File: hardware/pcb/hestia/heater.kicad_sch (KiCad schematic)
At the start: 23 parts, among them Q1 FDS8876, SW2 SW_Push_Open, U10 INA826

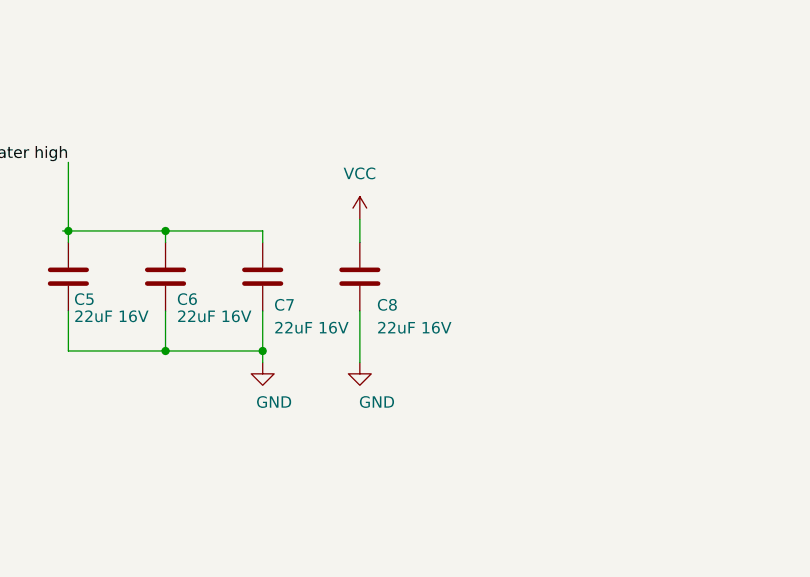
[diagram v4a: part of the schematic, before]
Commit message: pcb: move C8 to buck_converter schematic, removed some outdated comments
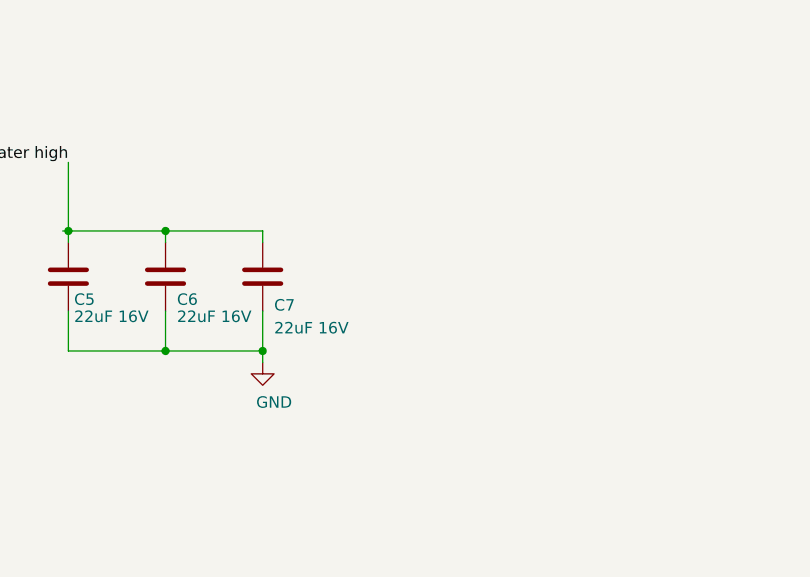
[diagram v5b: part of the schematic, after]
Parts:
- removed C8: 22uF 16V, Capacitor_SMD:C_1206_3216Metric, symbol Device:C
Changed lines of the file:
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@@
-    (stroke (width 0) (type default) (color 0 0 0 0))
-  )
-  (wire (pts (xy 239.395 57.785) (xy 239.395 60.325))
     (stroke (width 0) (type default) (color 0 0 0 0))
   )
@@
   )
   (wire (pts (xy 217.805 67.945) (xy 217.805 72.39))
-    (stroke (width 0) (type default) (color 0 0 0 0))
-  )
-  (wire (pts (xy 239.395 67.945) (xy 239.395 73.66))
     (stroke (width 0) (type default) (color 0 0 0 0))
   )
@@
     (pin "1")
   )
-  (symbol (lib_id "power:VCC") (at 239.395 57.785 0) (unit 1)
-    (in_bom yes) (on_board yes) (fields_autoplaced)
-    (property "Reference" "#PWR07" (id 0) (at 239.395 61.595 0)
-      (effects (font (size 1.27 1.27)) hide)
-    )
-    (property "Value" "VCC" (id 1) (at 239.395 52.705 0))
-    (property "Footprint" "" (id 2) (at 239.395 57.785 0)
-      (effects (font (size 1.27 1.27)) hide)
-    )
-    (property "Datasheet" "" (id 3) (at 239.395 57.785 0)
-      (effects (font (size 1.27 1.27)) hide)
-    )
-    (pin "1")
-  )
   (symbol (lib_id "power:VCC") (at 129.54 73.66 0) (unit 1)
     (in_bom yes) (on_board yes) (fields_autoplaced)
@@
     )
     (pin "1")
-  )
-  (symbol (lib_id "Device:C") (at 239.395 64.135 0) (unit 1)
-    (in_bom yes) (on_board yes)
-    (property "Reference" "C8" (id 0) (at 241.3 67.31 0)
-      (effects (font (size 1.27 1.27)) (justify left))
-    )
-    (property "Value" "22uF 16V" (id 1) (at 241.3 69.85 0)
-      (effects (font (size 1.27 1.27)) (justify left))
-    )
-    (property "Footprint" "Capacitor_SMD:C_1206_3216Metric" (id 2) (at 240.3602 67.945 0)
-      (effects (font (size 1.27 1.27)) hide)
-    )
-    (property "Datasheet" "~" (id 3) (at 239.395 64.135 0)
-      (effects (font (size 1.27 1.27)) hide)
-    )
-    (property "LCSC Part" "C13585" (id 4) (at 239.395 64.135 0)
-      (effects (font (size 1.27 1.27)) hide)
-    )
-    (pin "1")
-    (pin "2")
   )
   (symbol (lib_id "Device:R") (at 106.045 122.555 90) (unit 1)
@@
     (pin "2")
   )
-  (symbol (lib_id "power:GND") (at 239.395 73.66 0) (unit 1)
-    (in_bom yes) (on_board yes)
-    (property "Reference" "#PWR08" (id 0) (at 239.395 80.01 0)
-      (effects (font (size 1.27 1.27)) hide)
-    )
-    (property "Value" "GND" (id 1) (at 241.3 78.105 0))
-    (property "Footprint" "" (id 2) (at 239.395 73.66 0)
-      (effects (font (size 1.27 1.27)) hide)
-    )
-    (property "Datasheet" "" (id 3) (at 239.395 73.66 0)
-      (effects (font (size 1.27 1.27)) hide)
-    )
-    (pin "1")
-  )
 )

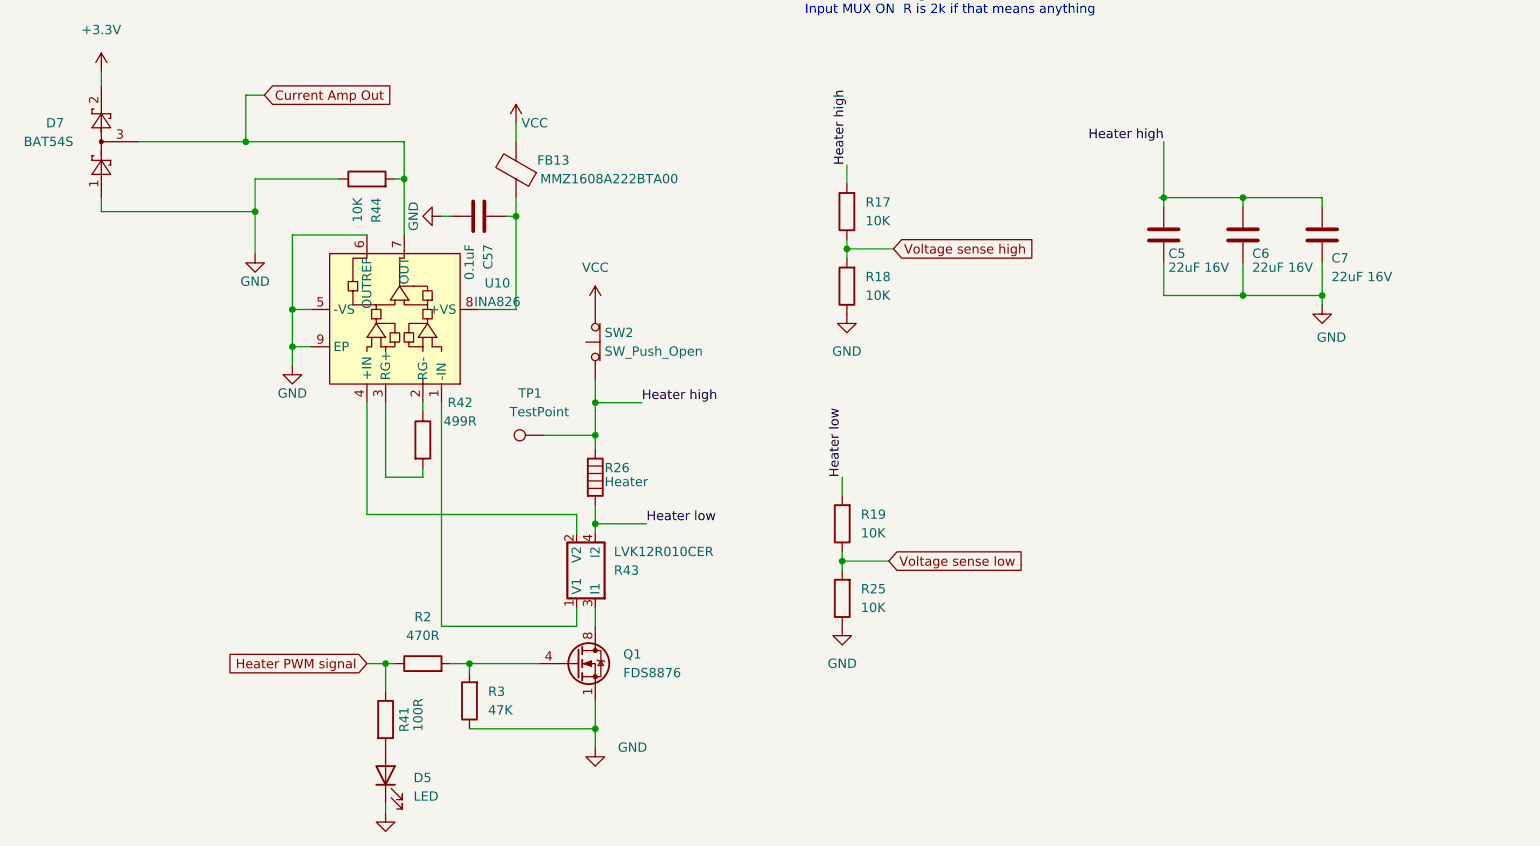
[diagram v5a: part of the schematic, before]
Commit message: added some digikey and mouser part numbers to schematic parts
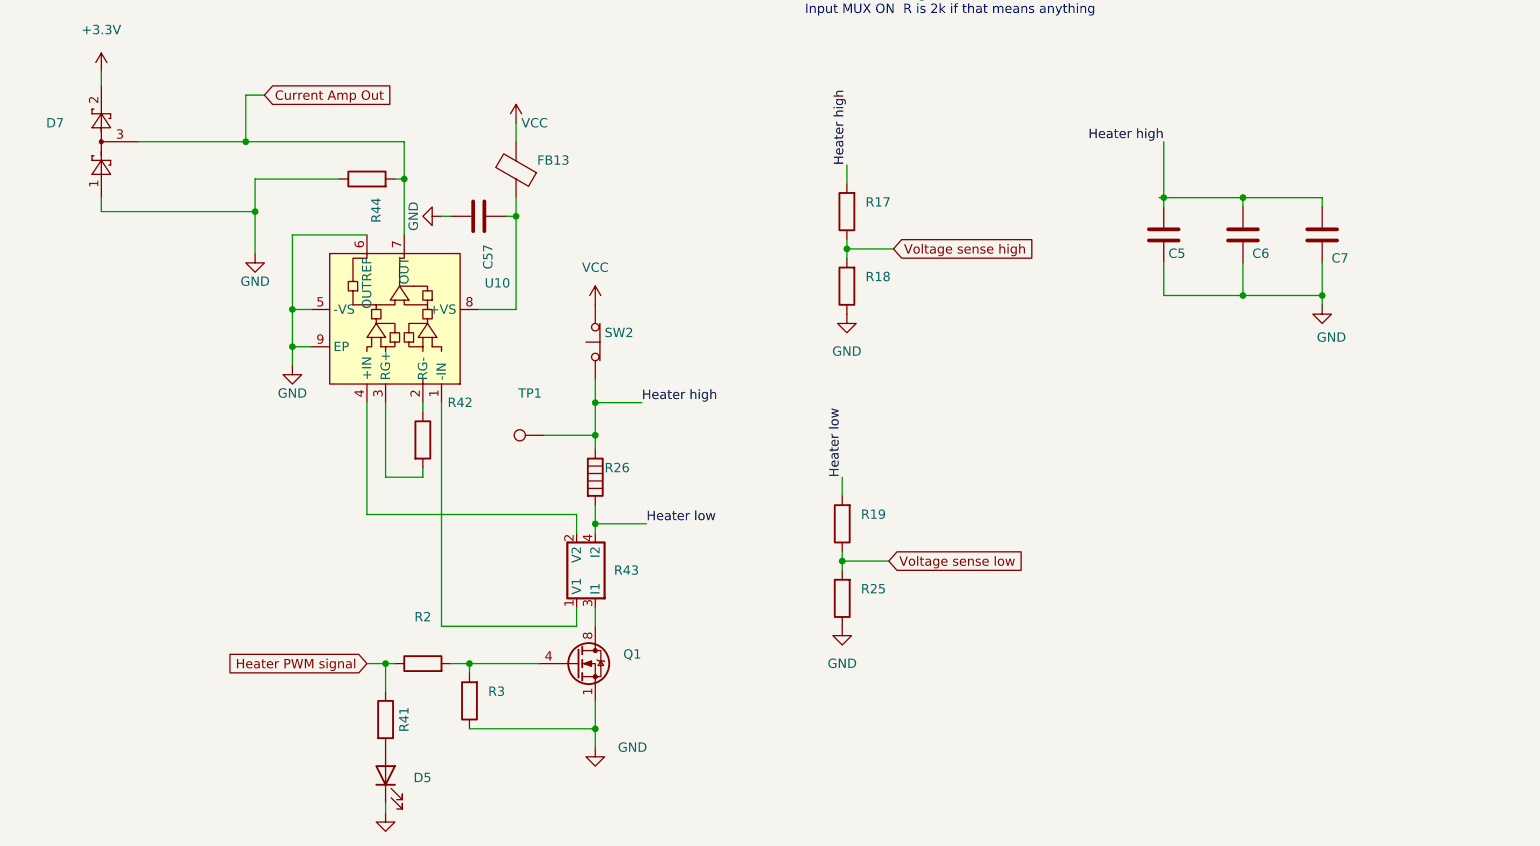
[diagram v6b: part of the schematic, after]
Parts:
- C5, C6, C7: value 22uF 16V -> (none); footprint Capacitor_SMD:C_1206_3216Metric -> (none); Digikey Part (none) -> 1276-2728-1-ND
- C57: value 0.1uF -> (none); footprint Capacitor_SMD:C_0603_1608Metric_Pad1.08x0.95mm_HandSolder -> (none)
- D5: value LED -> (none); footprint LED_SMD:LED_0805_2012Metric_Pad1.15x1.40mm_HandSolder -> (none)
- D7: value BAT54S -> (none); footprint Package_TO_SOT_SMD:SOT-23 -> (none); Digikey Part (none) -> BAT54SWT1GOSCT-ND
- FB13: value MMZ1608A222BTA00 -> (none); footprint Resistor_SMD:R_0603_1608Metric_Pad0.98x0.95mm_HandSolder -> (none); Mouser Part (none) -> 810-MMZ1608A222BTA00
- Q1: value FDS8876 -> (none); footprint Package_SO:SOIC-8_3.9x4.9mm_P1.27mm -> (none); Mouser Part (none) -> 512-FDS8876
- R17, R18, R19, R25, R44: value 10K -> (none); footprint Resistor_SMD:R_0603_1608Metric_Pad0.98x0.95mm_HandSolder -> (none)
- R2: value 470R -> (none); footprint Resistor_SMD:R_0603_1608Metric_Pad0.98x0.95mm_HandSolder -> (none)
- R26: value Heater -> (none); footprint NetTie:NetTie-2_SMD_Pad0.5mm -> (none)
- R3: value 47K -> (none); footprint Resistor_SMD:R_0603_1608Metric_Pad0.98x0.95mm_HandSolder -> (none)
- R41: value 100R -> (none); footprint Resistor_SMD:R_0603_1608Metric_Pad0.98x0.95mm_HandSolder -> (none)
- R42: value 499R -> (none); footprint Capacitor_SMD:C_0402_1005Metric -> (none)
- R43: value LVK12R010CER -> (none); footprint Hestia:LVK12R010CER -> (none); Digikey Part (none) -> 273-LVK12R010CERCT-ND
- SW2: value SW_Push_Open -> (none); footprint Connector_PinHeader_2.54mm:PinHeader_1x02_P2.54mm_Vertical -> (none)
- TP1: value TestPoint -> (none); footprint TestPoint:TestPoint_Pad_2.0x2.0mm -> (none)
- U10: value INA826 -> (none); footprint Package_SON:WSON-8-1EP_3x3mm_P0.5mm_EP1.2x2mm -> (none); Digikey Part (none) -> 296-36596-1-ND

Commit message: added more digikey part numbers to schematic
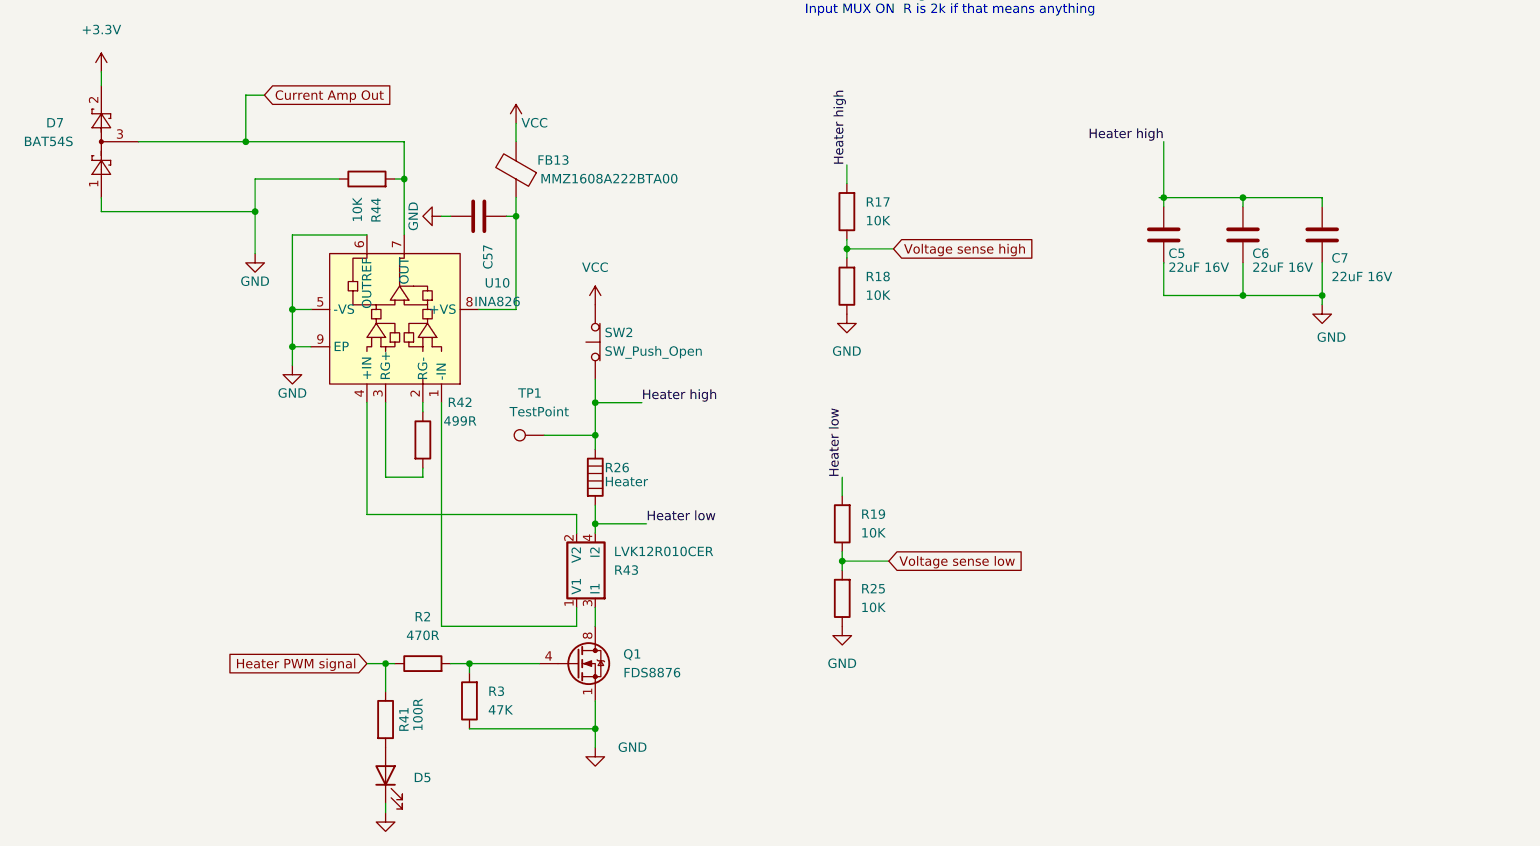
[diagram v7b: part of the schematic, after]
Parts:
- C5, C6, C7: value (none) -> 22uF 16V; footprint (none) -> Capacitor_SMD:C_1206_3216Metric
- C57: Digikey Part (none) -> 1276-CL10B104KB8WPNDCT-ND
- D7: value (none) -> BAT54S; footprint (none) -> Package_TO_SOT_SMD:SOT-23
- FB13: value (none) -> MMZ1608A222BTA00; footprint (none) -> Resistor_SMD:R_0603_1608Metric_Pad0.98x0.95mm_HandSolder
- Q1: value (none) -> FDS8876; footprint (none) -> Package_SO:SOIC-8_3.9x4.9mm_P1.27mm
- R17, R18, R19, R25, R44: value (none) -> 10K; footprint (none) -> Resistor_SMD:R_0603_1608Metric_Pad0.98x0.95mm_HandSolder
- R2: value (none) -> 470R; footprint (none) -> Resistor_SMD:R_0603_1608Metric_Pad0.98x0.95mm_HandSolder
- R26: value (none) -> Heater; footprint (none) -> NetTie:NetTie-2_SMD_Pad0.5mm
- R3: value (none) -> 47K; footprint (none) -> Resistor_SMD:R_0603_1608Metric_Pad0.98x0.95mm_HandSolder
- R41: value (none) -> 100R; footprint (none) -> Resistor_SMD:R_0603_1608Metric_Pad0.98x0.95mm_HandSolder
- R42: value (none) -> 499R; footprint (none) -> Capacitor_SMD:C_0402_1005Metric
- R43: value (none) -> LVK12R010CER; footprint (none) -> Hestia:LVK12R010CER
- SW2: value (none) -> SW_Push_Open; footprint (none) -> Connector_PinHeader_2.54mm:PinHeader_1x02_P2.54mm_Vertical
- TP1: value (none) -> TestPoint; footprint (none) -> TestPoint:TestPoint_Pad_2.0x2.0mm
- U10: value (none) -> INA826; footprint (none) -> Package_SON:WSON-8-1EP_3x3mm_P0.5mm_EP1.2x2mm

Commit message: added more digikey part numbers to schematic
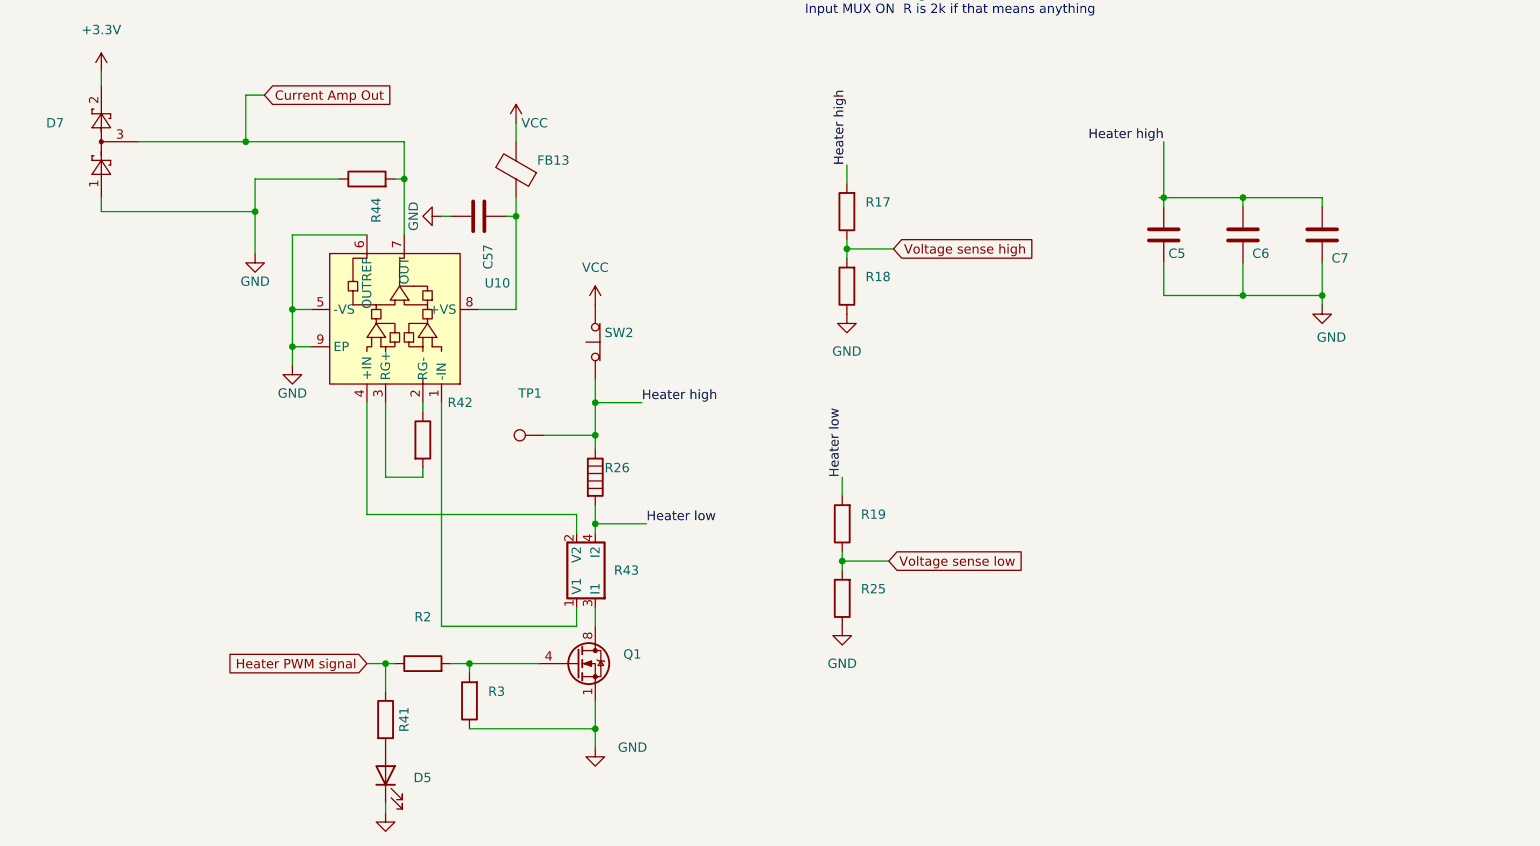
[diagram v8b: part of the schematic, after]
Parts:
- C5, C6, C7: value 22uF 16V -> (none); footprint Capacitor_SMD:C_1206_3216Metric -> (none)
- D7: value BAT54S -> (none); footprint Package_TO_SOT_SMD:SOT-23 -> (none)
- FB13: value MMZ1608A222BTA00 -> (none); footprint Resistor_SMD:R_0603_1608Metric_Pad0.98x0.95mm_HandSolder -> (none)
- Q1: value FDS8876 -> (none); footprint Package_SO:SOIC-8_3.9x4.9mm_P1.27mm -> (none)
- R17, R18, R19, R25, R44: value 10K -> (none); footprint Resistor_SMD:R_0603_1608Metric_Pad0.98x0.95mm_HandSolder -> (none)
- R2: value 470R -> (none); footprint Resistor_SMD:R_0603_1608Metric_Pad0.98x0.95mm_HandSolder -> (none); Digikey Part (none) -> RHM470ADCT-ND
- R26: value Heater -> (none); footprint NetTie:NetTie-2_SMD_Pad0.5mm -> (none)
- R3: value 47K -> (none); footprint Resistor_SMD:R_0603_1608Metric_Pad0.98x0.95mm_HandSolder -> (none); Digikey Part (none) -> P47KBZCT-ND
- R41: value 100R -> (none); footprint Resistor_SMD:R_0603_1608Metric_Pad0.98x0.95mm_HandSolder -> (none)
- R42: value 499R -> (none); footprint Capacitor_SMD:C_0402_1005Metric -> (none)
- R43: value LVK12R010CER -> (none); footprint Hestia:LVK12R010CER -> (none)
- SW2: value SW_Push_Open -> (none); footprint Connector_PinHeader_2.54mm:PinHeader_1x02_P2.54mm_Vertical -> (none)
- TP1: value TestPoint -> (none); footprint TestPoint:TestPoint_Pad_2.0x2.0mm -> (none)
- U10: value INA826 -> (none); footprint Package_SON:WSON-8-1EP_3x3mm_P0.5mm_EP1.2x2mm -> (none)
